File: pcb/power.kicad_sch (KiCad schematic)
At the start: 10 parts

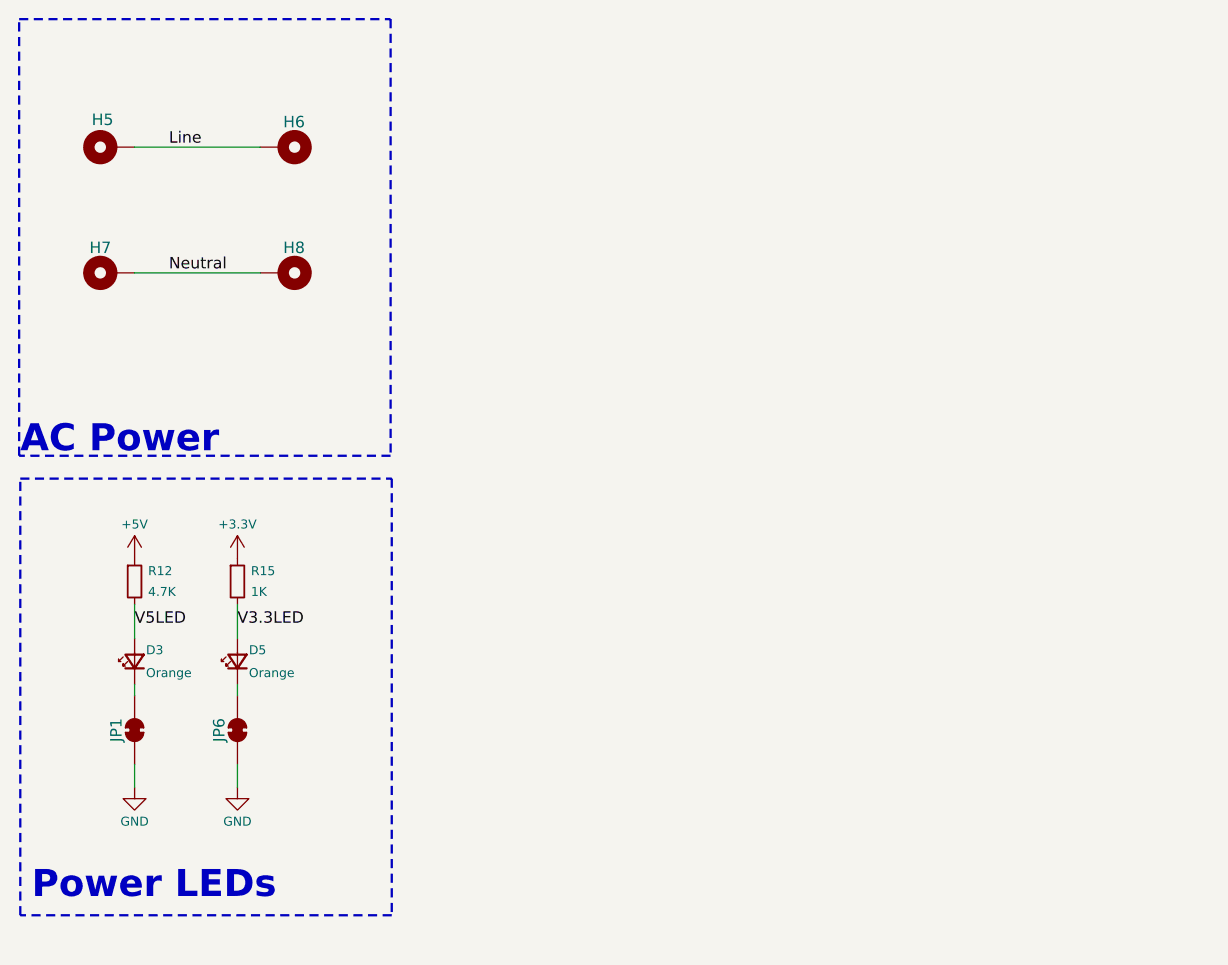
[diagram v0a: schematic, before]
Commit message: Updates for consistency
Changed mounting holes to grounded
Updated power connectors
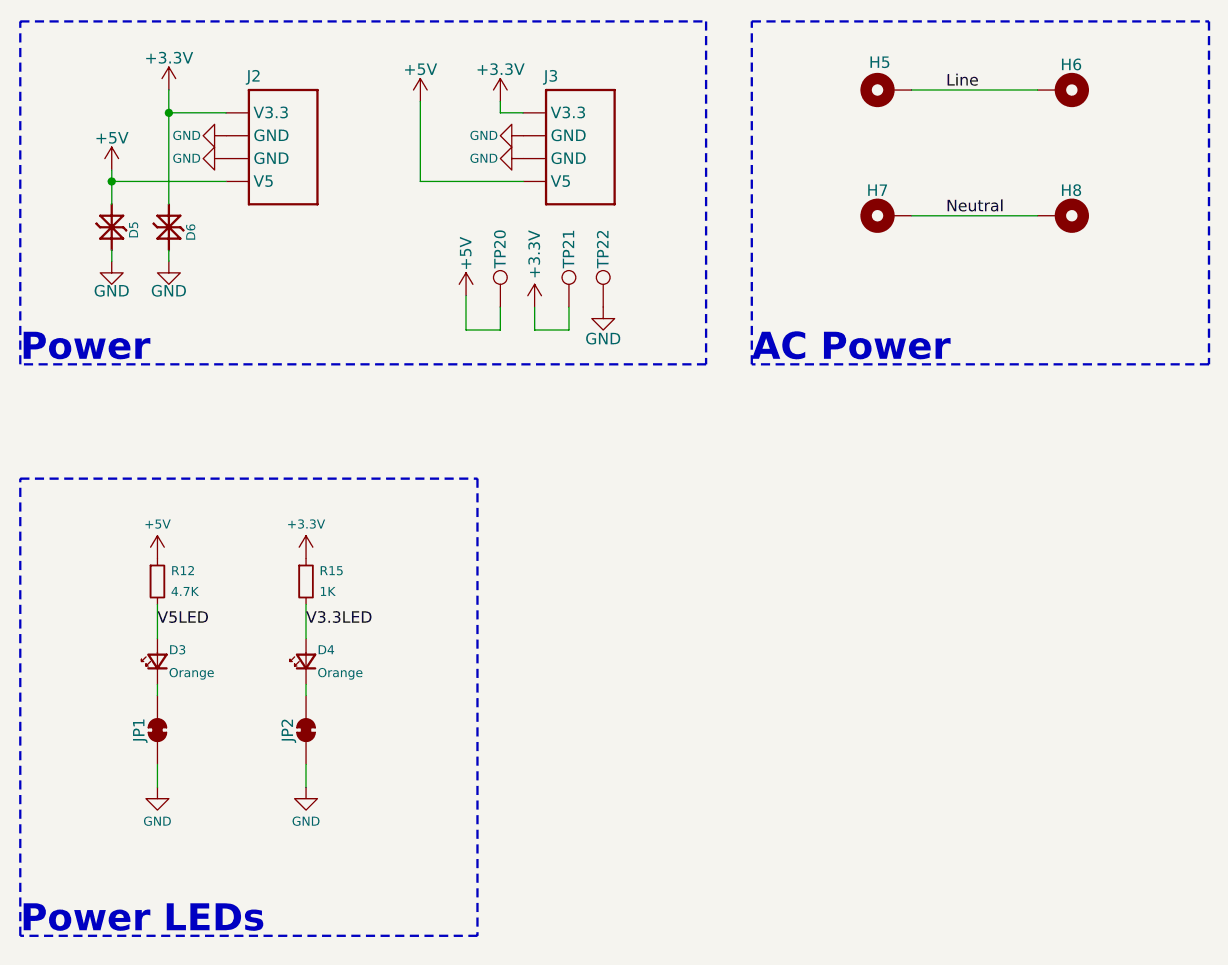
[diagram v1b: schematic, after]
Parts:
- removed D5: Orange, CRGM Passive:LED_0603_1608Metric, symbol Device:LED_Small
- removed JP6: ~, CRGM Connector:SolderJumper-2_P1.3mm_Bridged_RoundedPad1.0x1.5mm, symbol Jumper:SolderJumper_2_Bridged
- added D4: Orange, CRGM Passive:LED_0603_1608Metric, symbol Device:LED_Small
- added D5: PESD5V5C1BL, CRGM Passive:DFN1006-2, symbol CRGM Passive:PESD5V5C1BLYL
- added D6: PESD3V3S1BL, CRGM Passive:DFN1006-2, symbol CRGM Passive:PESD3V3S1BL
- added J2, J3: ~, CRGM Connector:JST_SH_SM04B-SRSS-TB_1x04-1MP_P1.00mm_Horizontal, symbol CRGM Connector:AQ_POWER
- added JP2: ~, CRGM Connector:SolderJumper-2_P1.3mm_Bridged_RoundedPad1.0x1.5mm, symbol Jumper:SolderJumper_2_Bridged
- added TP20, TP21, TP22: ~, CRGM Mechanical:TestPoint_Pad_D1.0mm, symbol Connector:TestPoint
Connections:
- net +3.3V: now also D6.2 (K2), J2.4 (V3.3), J3.4 (V3.3), TP21.1
- net +5V: now also D5.2 (K2), J2.1 (V5), J3.1 (V5), TP20.1
- net GND: now also D5.1 (K1), D6.1 (K1), J2.2 (GND), J2.3 (GND), J3.2 (GND), J3.3 (GND), JP2.1 (A), TP22.1
- net V3.3LED: now also D4.2 (A)
- new net: D4.1 (K), JP2.2 (B)
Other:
- note added: "Power"
- moved on the sheet: D3, H5, H6, H7, H8, JP1, R12, R15

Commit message: Swapped parts based on availability
Added additional filtering caps
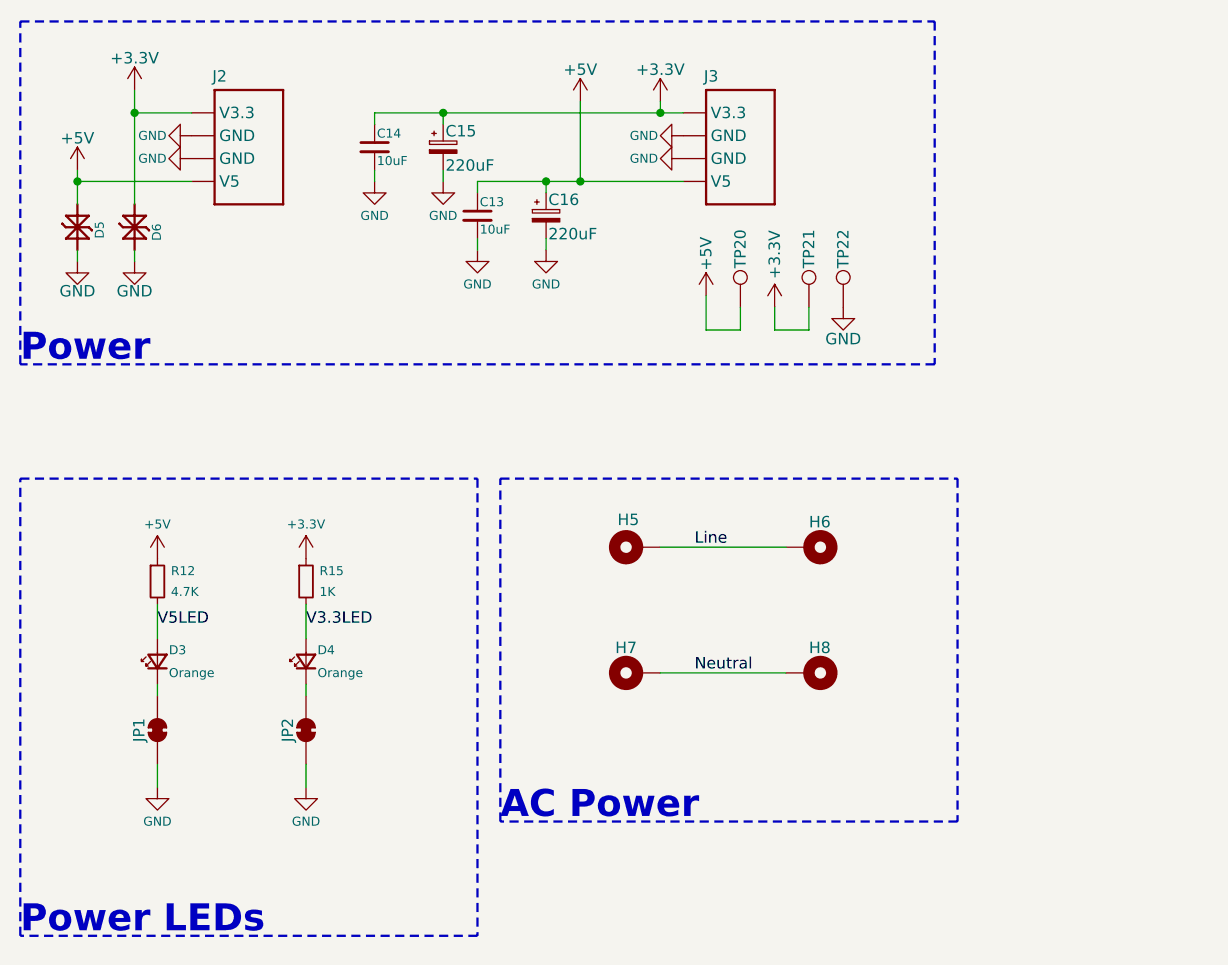
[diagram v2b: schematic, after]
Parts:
- added C13, C14: 10uF, CRGM Passive:C_0603_1608Metric, symbol Device:C_Small
- added C15, C16: 220uF, CRGM Passive:CP_Elec_6.3x5.4, symbol Device:C_Polarized_Small
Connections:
- net +3.3V: now also C14.1, C15.1
- net +5V: now also C13.1, C16.1
- net GND: now also C13.2, C14.2, C15.2, C16.2
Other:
- moved on the sheet: D5, D6, H5, H6, H7, H8, J2, J3, TP20, TP21, TP22

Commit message: Removed power connectors
Removed power connector as 5v is not necessary.
Added 100uF caps to power
Added TVS to I2C and VOUT
Rerouted entire board
Adjusted silkscreen
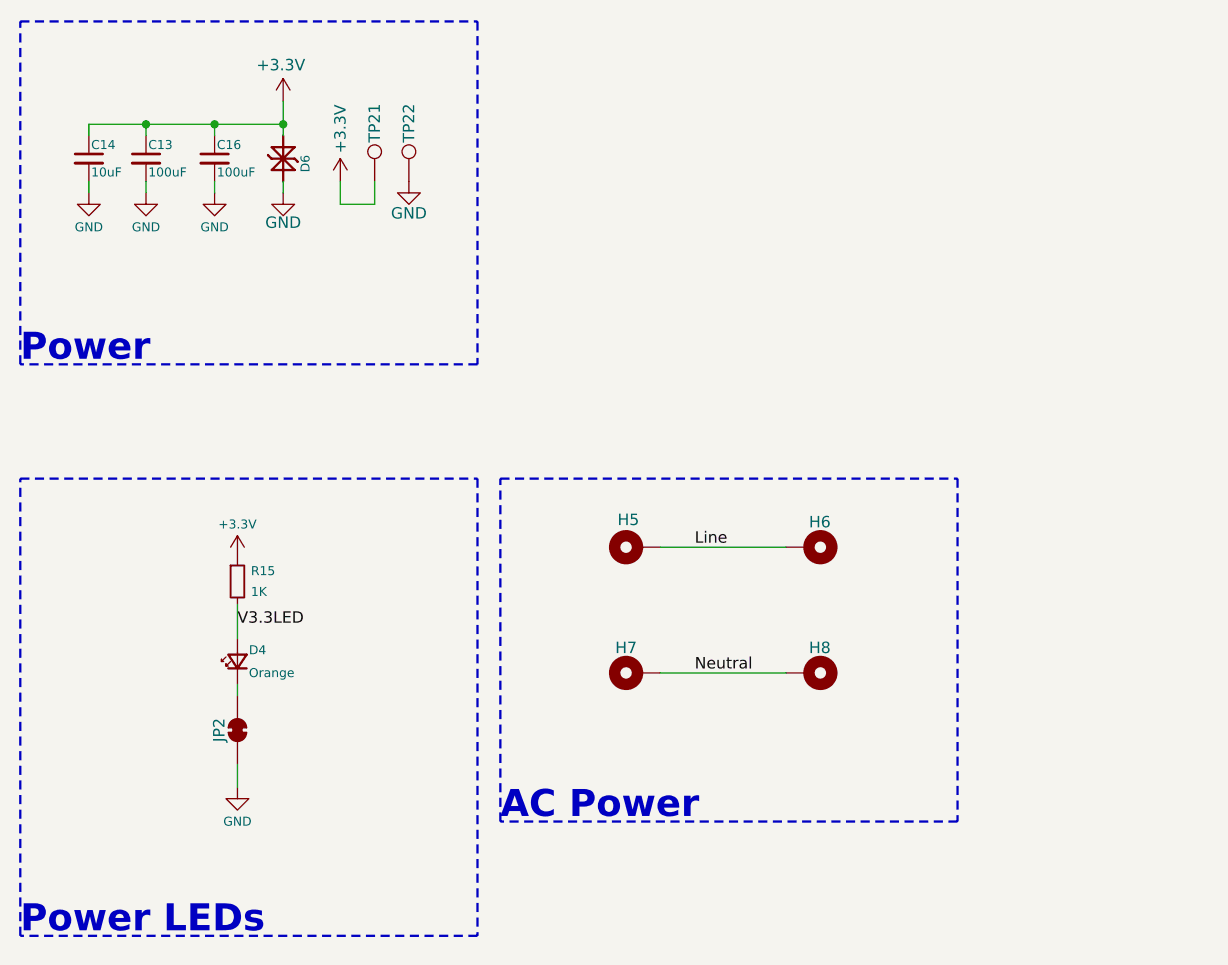
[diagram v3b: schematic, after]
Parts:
- removed C15, C16: 220uF, CRGM Passive:CP_Elec_6.3x5.4, symbol Device:C_Polarized_Small
- removed D3: Orange, CRGM Passive:LED_0603_1608Metric, symbol Device:LED_Small
- removed D5: PESD5V5C1BL, CRGM Passive:DFN1006-2, symbol CRGM Passive:PESD5V5C1BLYL
- removed J2, J3: ~, CRGM Connector:JST_SH_SM04B-SRSS-TB_1x04-1MP_P1.00mm_Horizontal, symbol CRGM Connector:AQ_POWER
- removed JP1: ~, CRGM Connector:SolderJumper-2_P1.3mm_Bridged_RoundedPad1.0x1.5mm, symbol Jumper:SolderJumper_2_Bridged
- removed R12: 4.7K, CRGM Passive:R_0603_1608Metric, symbol Device:R_Small
- removed TP20: ~, CRGM Mechanical:TestPoint_Pad_D1.0mm, symbol Connector:TestPoint
- added C16: 100uF, CRGM Passive:C_1206_3216Metric, symbol Device:C_Small
- C13: value 10uF -> 100uF; footprint CRGM Passive:C_0603_1608Metric -> CRGM Passive:C_1206_3216Metric; Digikey 1276-1870-2-ND -> 1276-1782-2-ND; LCSC C92487 -> C15008; MPN CL10A106MO8NQNC -> CL31A107MQHNNNE; Mouser 187-CL10A106MO8NQNC -> 187-CL31A107MQHNNNE; Tolerance 10% -> 20%
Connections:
- net +5V is gone; now on net +3.3V: C13.1
- net +3.3V: now also C16.1
- net GND: now also C16.2
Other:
- moved on the sheet: C14, D4, D6, JP2, R15, TP21, TP22

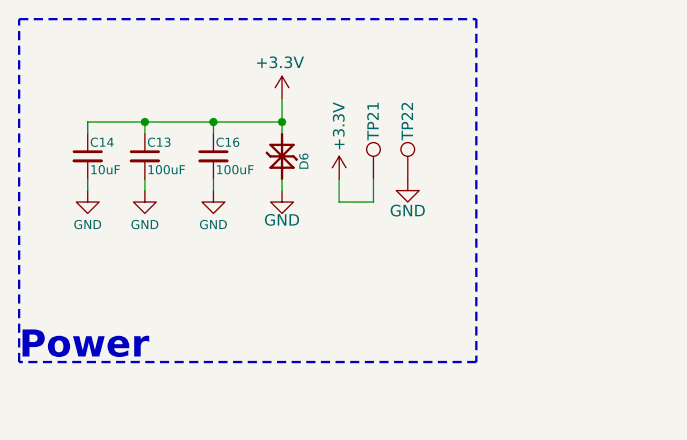
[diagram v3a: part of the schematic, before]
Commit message: Collapsed UPDI and Serial
Added indicator LEDs
Rerouted
Cleaned up silkscreen
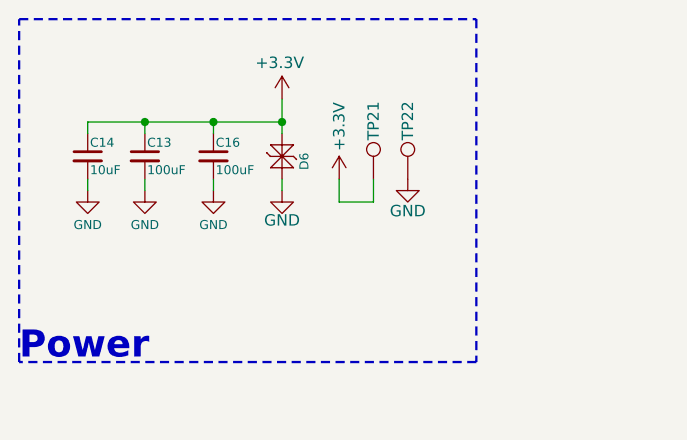
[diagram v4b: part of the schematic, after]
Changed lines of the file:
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@@
+			)
+		)
+		(property "Sim.Enable" ""
+			(at 49.53 104.14 0)
+			(effects
+				(font
+					(size 1.27 1.27)
+				)
+				(hide yes)
 			)
 		)
@@
 			)
 		)
+		(property "Sim.Enable" ""
+			(at 93.98 83.82 90)
+			(effects
+				(font
+					(size 1.27 1.27)
+				)
+				(hide yes)
+			)
+		)
 		(pin "1"
 		)
@@
 			)
 		)
+		(property "Sim.Enable" ""
+			(at 54.61 40.64 0)
+			(effects
+				(font
+					(size 1.27 1.27)
+				)
+				(hide yes)
+			)
+		)
 		(pin "1"
 		)
@@
 			)
 		)
+		(property "Sim.Enable" ""
+			(at 113.03 83.82 90)
+			(effects
+				(font
+					(size 1.27 1.27)
+				)
+				(hide yes)
+			)
+		)
 		(pin "1"
 		)
@@
 			)
 		)
+		(property "Sim.Enable" ""
+			(at 93.98 97.79 90)
+			(effects
+				(font
+					(size 1.27 1.27)
+				)
+				(hide yes)
+			)
+		)
 		(pin "1"
 		)
@@
 			)
 		)
-		(property "Datasheet" "https://optoelectronics.liteon.com/upload/download/DS22-2000-228/LTST-C191KGKT.PDF"
+		(property "Datasheet" "~"
 			(at 49.53 96.52 0)
 			(effects
@@
 			)
 		)
-		(property "Description" "20mA 315mcd Colorless Orange 120° 50mW 2.3V 0603"
+		(property "Description" "Light emitting diode, small symbol"
 			(at 49.53 96.52 0)
 			(effects
@@
 					(size 1 1)
 					(color 223 129 255 1)
+				)
+				(hide yes)
+			)
+		)
+		(property "Sim.Pins" "1=K 2=A"
+			(at 49.53 96.52 0)
+			(effects
+				(font
+					(size 1.27 1.27)
+				)
+				(hide yes)
+			)
+		)
+		(property "Sim.Enable" ""
+			(at 49.53 96.52 90)
+			(effects
+				(font
+					(size 1.27 1.27)
 				)
 				(hide yes)
@@
 			)
 		)
-		(property "Datasheet" "https://mm.digikey.com/Volume0/opasdata/d220001/medias/docus/43/CL10A106MO8NQNC_Spec.pdf"
+		(property "Datasheet" "~"
 			(at 46.99 40.64 0)
 			(effects
@@
 			)
 		)
-		(property "Description" "100uF 6.3V X5R ±20% 1206 Multilayer Ceramic Capacitors MLCC"
+		(property "Description" "Unpolarized capacitor, small symbol"
 			(at 46.99 40.64 0)
 			(effects
@@
 		)
 		(property "Package" ""
+			(at 46.99 40.64 0)
+			(effects
+				(font
+					(size 1.27 1.27)
+				)
+				(hide yes)
+			)
+		)
+		(property "Sim.Enable" ""
 			(at 46.99 40.64 0)
 			(effects
@@
 			)
 		)
-		(property "Description" ""
+		(property "Description" "Power symbol creates a global label with name \"GND\" , ground"
 			(at 49.53 110.49 0)
 			(effects
@@
 			)
 		)
-		(property "Description" "test point"
+		(property "Description" "Test Point D1.0mm"
 			(at 64.77 43.18 0)
 			(effects
@@
 		(property "Mouser" ""
 			(at 64.77 43.18 0)
+			(effects
+				(font
+					(size 1.27 1.27)
+				)
+				(hide yes)
+			)
+		)
+		(property "Sim.Enable" ""
+			(at 64.77 43.18 90)
 			(effects
 				(font
@@
 			)
 		)
-		(property "Description" ""
+		(property "Description" "Power symbol creates a global label with name \"+3.3V\""
 			(at 49.53 85.09 0)
 			(effects
@@
 			)
 		)
-		(property "Description" "test point"
+		(property "Description" "Test Point D1.0mm"
 			(at 68.58 43.18 0)
 			(effects
@@
 		(property "Mouser" ""
 			(at 68.58 43.18 0)
+			(effects
+				(font
+					(size 1.27 1.27)
+				)
+				(hide yes)
+			)
+		)
+		(property "Sim.Enable" ""
+			(at 68.58 43.18 90)
 			(effects
 				(font
@@
 			)
 		)
-		(property "Datasheet" "https://mm.digikey.com/Volume0/opasdata/d220001/medias/docus/43/CL10A106MO8NQNC_Spec.pdf"
+		(property "Datasheet" "~"
 			(at 33.02 40.64 0)
 			(effects
@@
 			)
 		)
-		(property "Description" "CAP CER 10uF 16V X5R 0603"
+		(property "Description" "Unpolarized capacitor, small symbol"
 			(at 33.02 40.64 0)
 			(effects
@@
 		)
 		(property "Tolerance" "10%"
+			(at 33.02 40.64 0)
+			(effects
+				(font
+					(size 1.27 1.27)
+				)
+				(hide yes)
+			)
+		)
+		(property "Sim.Enable" ""
 			(at 33.02 40.64 0)
 			(effects
@@
 			)
 		)
-		(property "Datasheet" "https://www.vishay.com/docs/28773/crcwce3.pdf"
+		(property "Datasheet" "~"
 			(at 49.53 87.63 0)
 			(effects
@@
 			)
 		)
-		(property "Description" "Thick Film Resistors - SMD 1/10watt 1.0Kohms 1%"
+		(property "Description" "Resistor, small symbol"
 			(at 49.53 87.63 0)
 			(effects
@@
 		)
 		(property "Tolerance" "5%"
+			(at 49.53 87.63 0)
+			(effects
+				(font
+					(size 1.27 1.27)
+				)
+				(hide yes)
+			)
+		)
+		(property "Sim.Enable" ""
 			(at 49.53 87.63 0)
 			(effects
@@
 			)
 		)
+		(property "Sim.Enable" ""
+			(at 113.03 97.79 90)
+			(effects
+				(font
+					(size 1.27 1.27)
+				)
+				(hide yes)
+			)
+		)
 		(pin "1"
 		)
@@
 			)
 		)
-		(property "Datasheet" "https://mm.digikey.com/Volume0/opasdata/d220001/medias/docus/43/CL10A106MO8NQNC_Spec.pdf"
+		(property "Datasheet" "~"
 			(at 39.37 40.64 0)
 			(effects
@@
 			)
 		)
-		(property "Description" "100uF 6.3V X5R ±20% 1206 Multilayer Ceramic Capacitors MLCC"
+		(property "Description" "Unpolarized capacitor, small symbol"
 			(at 39.37 40.64 0)
 			(effects
@@
 			(at 39.37 40.64 0)
 			(effects
+				(font
+					(size 1.27 1.27)
+				)
+				(hide yes)
+			)
+		)
+		(property "Sim.Enable" ""
+			(at 39.37 40.64 0)
+			(effects
